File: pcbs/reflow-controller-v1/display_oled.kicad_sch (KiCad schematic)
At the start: 7 parts, among them J801 SSD1306 white module

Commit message: kicad version bump
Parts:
- R801, R802: value 4.7k -> 3k3

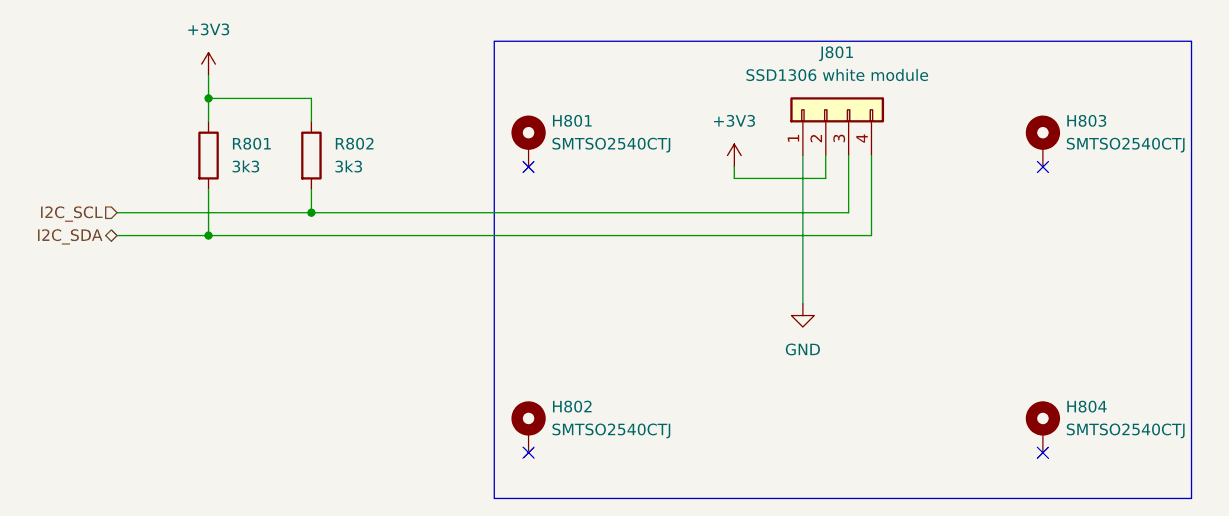
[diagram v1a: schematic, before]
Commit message: footprint assignement fixed; buzzer added
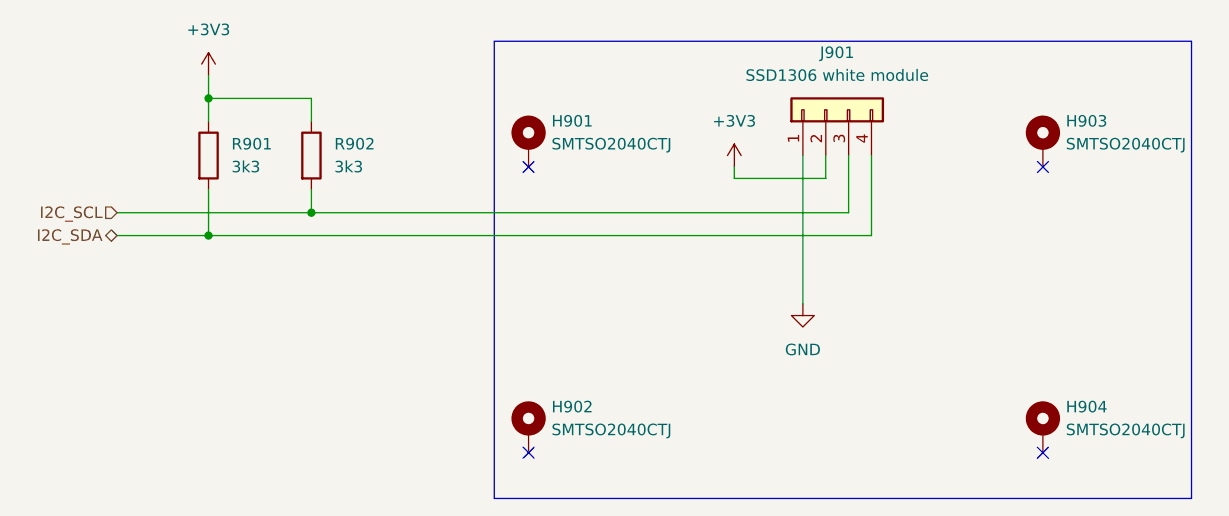
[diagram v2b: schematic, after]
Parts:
- H901: renamed from H801; value SMTSO2540CTJ -> SMTSO2040CTJ; footprint WA-SMSI_M2.5:Mounting_Wuerth_WA-SMSI-M2.5_H4mm_9774040151 -> Mounting_Wuerth:Mounting_Wuerth_WA-SMSI-M2_H4mm_9774040243
- H902: renamed from H802; value SMTSO2540CTJ -> SMTSO2040CTJ; footprint WA-SMSI_M2.5:Mounting_Wuerth_WA-SMSI-M2.5_H4mm_9774040151 -> Mounting_Wuerth:Mounting_Wuerth_WA-SMSI-M2_H4mm_9774040243
- H903: renamed from H803; value SMTSO2540CTJ -> SMTSO2040CTJ; footprint WA-SMSI_M2.5:Mounting_Wuerth_WA-SMSI-M2.5_H4mm_9774040151 -> Mounting_Wuerth:Mounting_Wuerth_WA-SMSI-M2_H4mm_9774040243
- H904: renamed from H804; value SMTSO2540CTJ -> SMTSO2040CTJ; footprint WA-SMSI_M2.5:Mounting_Wuerth_WA-SMSI-M2.5_H4mm_9774040151 -> Mounting_Wuerth:Mounting_Wuerth_WA-SMSI-M2_H4mm_9774040243
- renumbered J801 to J901, R801 to R901, R802 to R902
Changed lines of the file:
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@@
 		(dnp no)
 		(fields_autoplaced yes)
-		(property "Reference" "#PWR0803"
+		(property "Reference" "#PWR0903"
 			(at 167.64 105.41 0)
 			(effects
@@
 		(dnp no)
 		(fields_autoplaced yes)
-		(property "Reference" "J801"
+		(property "Reference" "J901"
 			(at 171.45 71.12 90)
 			(effects
@@
 		(dnp no)
 		(fields_autoplaced yes)
-		(property "Reference" "R802"
+		(property "Reference" "R902"
 			(at 115.57 81.28 0)
 			(effects
@@
 		(dnp no)
 		(fields_autoplaced yes)
-		(property "Reference" "H801"
-			(at 139.7 78.74 0)
-			(effects
-				(font
-					(size 1.27 1.27)
-				)
-				(justify left)
-			)
-		)
-		(property "Value" "SMTSO2540CTJ"
-			(at 139.7 81.28 0)
-			(effects
-				(font
-					(size 1.27 1.27)
-				)
-				(justify left)
-			)
-		)
-		(property "Footprint" "WA-SMSI_M2.5:Mounting_Wuerth_WA-SMSI-M2.5_H4mm_9774040151"
+		(property "Reference" "H901"
+			(at 139.7 78.7399 0)
+			(effects
+				(font
+					(size 1.27 1.27)
+				)
+				(justify left)
+			)
+		)
+		(property "Value" "SMTSO2040CTJ"
+			(at 139.7 81.2799 0)
+			(effects
+				(font
+					(size 1.27 1.27)
+				)
+				(justify left)
+			)
+		)
+		(property "Footprint" "Mounting_Wuerth:Mounting_Wuerth_WA-SMSI-M2_H4mm_9774040243"
 			(at 137.16 81.28 0)
 			(effects
@@
 		(dnp no)
 		(fields_autoplaced yes)
-		(property "Reference" "H802"
-			(at 139.7 110.49 0)
-			(effects
-				(font
-					(size 1.27 1.27)
-				)
-				(justify left)
-			)
-		)
-		(property "Value" "SMTSO2540CTJ"
-			(at 139.7 113.03 0)
-			(effects
-				(font
-					(size 1.27 1.27)
-				)
-				(justify left)
-			)
-		)
-		(property "Footprint" "WA-SMSI_M2.5:Mounting_Wuerth_WA-SMSI-M2.5_H4mm_9774040151"
+		(property "Reference" "H902"
+			(at 139.7 110.4899 0)
+			(effects
+				(font
+					(size 1.27 1.27)
+				)
+				(justify left)
+			)
+		)
+		(property "Value" "SMTSO2040CTJ"
+			(at 139.7 113.0299 0)
+			(effects
+				(font
+					(size 1.27 1.27)
+				)
+				(justify left)
+			)
+		)
+		(property "Footprint" "Mounting_Wuerth:Mounting_Wuerth_WA-SMSI-M2_H4mm_9774040243"
 			(at 137.16 113.03 0)
 			(effects
@@
 		(dnp no)
 		(fields_autoplaced yes)
-		(property "Reference" "H803"
-			(at 196.85 78.74 0)
-			(effects
-				(font
-					(size 1.27 1.27)
-				)
-				(justify left)
-			)
-		)
-		(property "Value" "SMTSO2540CTJ"
-			(at 196.85 81.28 0)
-			(effects
-				(font
-					(size 1.27 1.27)
-				)
-				(justify left)
-			)
-		)
-		(property "Footprint" "WA-SMSI_M2.5:Mounting_Wuerth_WA-SMSI-M2.5_H4mm_9774040151"
+		(property "Reference" "H903"
+			(at 196.85 78.7399 0)
+			(effects
+				(font
+					(size 1.27 1.27)
+				)
+				(justify left)
+			)
+		)
+		(property "Value" "SMTSO2040CTJ"
+			(at 196.85 81.2799 0)
+			(effects
+				(font
+					(size 1.27 1.27)
+				)
+				(justify left)
+			)
+		)
+		(property "Footprint" "Mounting_Wuerth:Mounting_Wuerth_WA-SMSI-M2_H4mm_9774040243"
 			(at 194.31 81.28 0)
 			(effects
@@
 		(dnp no)
 		(fields_autoplaced yes)
-		(property "Reference" "#PWR0802"
+		(property "Reference" "#PWR0902"
 			(at 160.02 87.63 0)
 			(effects
@@
 		(dnp no)
 		(fields_autoplaced yes)
-		(property "Reference" "#PWR0801"
+		(property "Reference" "#PWR0901"
 			(at 101.6 77.47 0)
 			(effects
@@
 		(dnp no)
 		(fields_autoplaced yes)
-		(property "Reference" "R801"
+		(property "Reference" "R901"
 			(at 104.14 81.28 0)
 			(effects
@@
 		(dnp no)
 		(fields_autoplaced yes)
-		(property "Reference" "H804"
-			(at 196.85 110.49 0)
-			(effects
-				(font
-					(size 1.27 1.27)
-				)
-				(justify left)
-			)
-		)
-		(property "Value" "SMTSO2540CTJ"
-			(at 196.85 113.03 0)
-			(effects
-				(font
-					(size 1.27 1.27)
-				)
-				(justify left)
-			)
-		)
-		(property "Footprint" "WA-SMSI_M2.5:Mounting_Wuerth_WA-SMSI-M2.5_H4mm_9774040151"
+		(property "Reference" "H904"
+			(at 196.85 110.4899 0)
+			(effects
+				(font
+					(size 1.27 1.27)
+				)
+				(justify left)
+			)
+		)
+		(property "Value" "SMTSO2040CTJ"
+			(at 196.85 113.0299 0)
+			(effects
+				(font
+					(size 1.27 1.27)
+				)
+				(justify left)
+			)
+		)
+		(property "Footprint" "Mounting_Wuerth:Mounting_Wuerth_WA-SMSI-M2_H4mm_9774040243"
 			(at 194.31 113.03 0)
 			(effects

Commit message: WIP pcb design & routing
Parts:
- removed H901, H902, H903, H904: SMTSO2040CTJ, Mounting_Wuerth:Mounting_Wuerth_WA-SMSI-M2_H4mm_9774040243, symbol Mechanical:MountingHole_Pad
- removed J901: SSD1306 white module, Connector_PinHeader_2.54mm:PinHeader_1x04_P2.54mm_Vertical, symbol Connector_Generic:Conn_01x04
- added U6: ~, display_modules:SSD1315 Module, symbol display_modules:SSD1315
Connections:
- net +3V3: now also U6.2 (VCC)
- net GND: now also U6.1 (GND)
- net I2C_SCL: now also U6.3 (SCL)
- net I2C_SDA: now also U6.4 (SDA)
- no-connect marks 4 -> 1

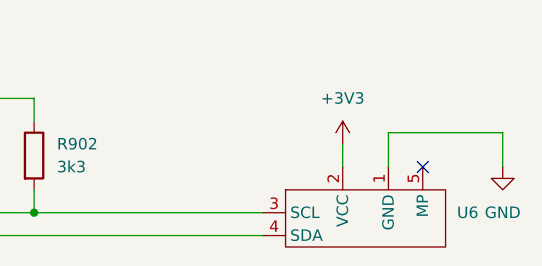
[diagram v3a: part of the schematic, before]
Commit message: update display placing & prelim. routing
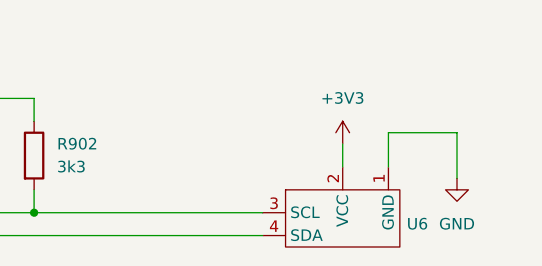
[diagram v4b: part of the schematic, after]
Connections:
- no-connect marks 1 -> 0
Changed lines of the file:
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@@
 		(color 0 0 0 0)
 	)
-	(no_connect
-		(at 156.21 83.82)
-	)
 	(wire
 		(pts
@@
 	(wire
 		(pts
-			(xy 165.1 80.01) (xy 165.1 83.82)
+			(xy 160.02 80.01) (xy 160.02 85.09)
 		)
 		(stroke
@@
 	(wire
 		(pts
-			(xy 152.4 80.01) (xy 165.1 80.01)
+			(xy 152.4 80.01) (xy 160.02 80.01)
 		)
 		(stroke
@@
 	(symbol
 		(lib_id "power:GND")
-		(at 165.1 83.82 0)
+		(at 160.02 85.09 0)
 		(unit 1)
 		(exclude_from_sim no)
@@
 		(fields_autoplaced yes)
 		(property "Reference" "#PWR0903"
-			(at 165.1 90.17 0)
+			(at 160.02 91.44 0)
 			(effects
 				(font
@@
 		)
 		(property "Value" "GND"
-			(at 165.1 88.9 0)
+			(at 160.02 90.17 0)
 			(effects
 				(font
@@
 		)
 		(property "Footprint" ""
-			(at 165.1 83.82 0)
+			(at 160.02 85.09 0)
 			(effects
 				(font
@@
 		)
 		(property "Datasheet" ""
-			(at 165.1 83.82 0)
-			(effects
-				(font
-					(size 1.27 1.27)
-				)
-				(hide yes)
-			)
-		)
-		(property "Description" ""
-			(at 165.1 83.82 0)
+			(at 160.02 85.09 0)
+			(effects
+				(font
+					(size 1.27 1.27)
+				)
+				(hide yes)
+			)
+		)
+		(property "Description" "Power symbol creates a global label with name \"GND\" , ground"
+			(at 160.02 85.09 0)
 			(effects
 				(font
@@
 			)
 		)
-		(property "Description" ""
+		(property "Description" "Resistor"
 			(at 113.03 82.55 0)
 			(effects
@@
 			)
 		)
-		(property "Description" ""
+		(property "Description" "Power symbol creates a global label with name \"+3V3\""
 			(at 147.32 81.28 0)
 			(effects
@@
 			)
 		)
-		(property "Description" ""
+		(property "Description" "Power symbol creates a global label with name \"+3V3\""
 			(at 101.6 73.66 0)
 			(effects
@@
 		(on_board yes)
 		(dnp no)
-		(fields_autoplaced yes)
 		(property "Reference" "U6"
-			(at 160.02 88.8999 0)
+			(at 154.432 90.17 0)
 			(effects
 				(font
@@
 		)
 		(pin "4"
-		)
-		(pin "5"
 		)
 		(pin "3"
@@
 			)
 		)
-		(property "Description" ""
+		(property "Description" "Resistor"
 			(at 101.6 82.55 0)
 			(effects
